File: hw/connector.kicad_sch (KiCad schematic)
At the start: 1 part, among them J1001 CONN_ECU_94

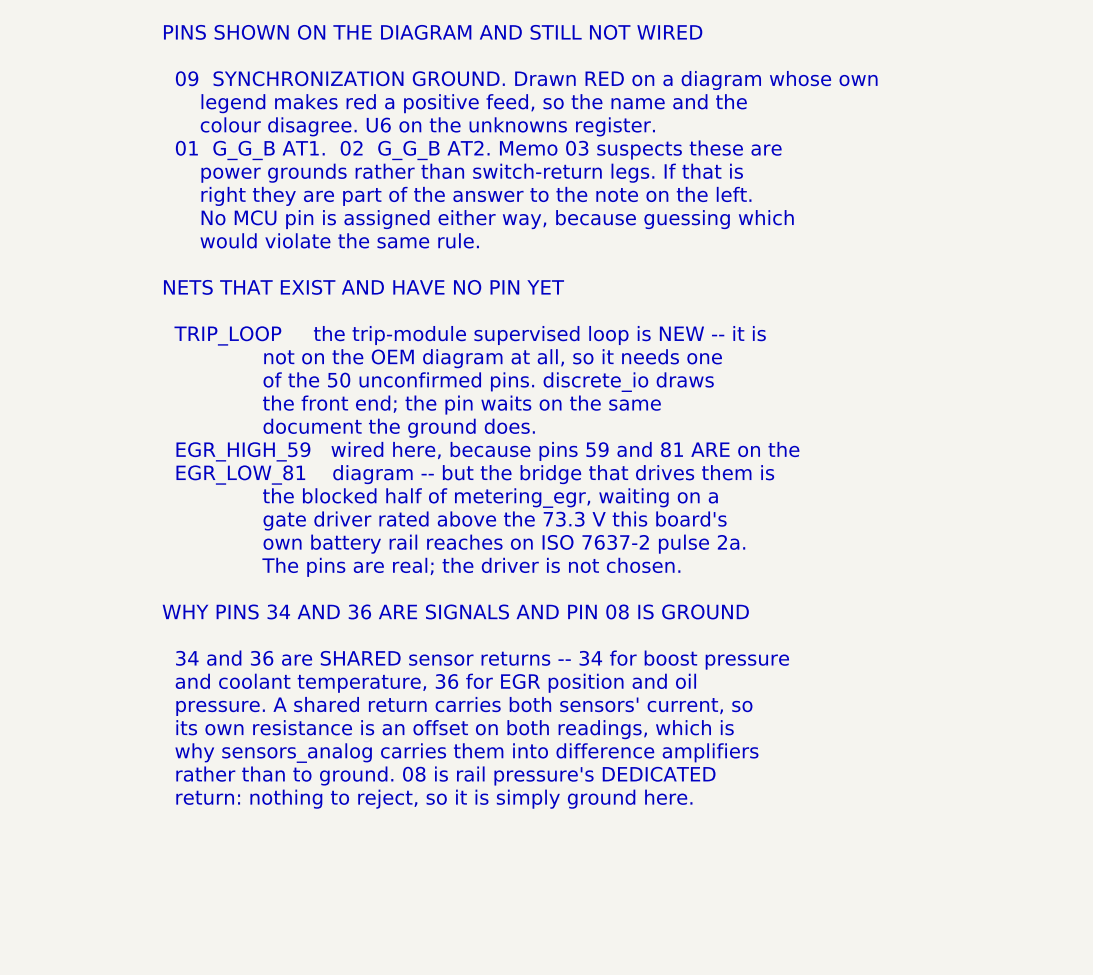
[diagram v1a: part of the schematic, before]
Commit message: Choose the buck inductor; record three design items the parts exposed
L201: Wurth 7447714330 (WE-PD 1050, 33 uH, Isat 2.9 A typ, AEC-Q200
Grade 1) -- 1.72x the 1.18 A worst peak after a -30% hot derate,
closing the Isat gap buck_preregulator.cir left open. Land pattern is
not in KiCad 7; phase 3.

Three items that are not part choices, each pinned as a check:
- POWER-PATH: injector and EGR current flows through pin 21, the EMI
  filter and a reverse FET sized for 5 A; pins 04/06 are 10 A battery
  feeds used only as senses. L101/L102/F101 wait on the decision.
- BOOST-SLOPE: by TI SLVS861F Eq. 9 the drawn 82 mOhm sense resistor
  exceeds the subharmonic ceiling at cranking (44.9 mOhm), and the
  330 uH it needs does not exist at a 2.2 A saturation rating.
- SENSOR-PTC: real PTCs are specified 0.40-5.00 ohm, not "3.0 ohm
  +/-30%", and Ihold halves at 85 C.

The netlist gate now counts the power ground as an open item: GND
reaches the connector only through sensor-ground pins. Removes a stale
EGR note from the connector sheet.

24/24 sim blocks, netlist gate passing with 2 named open items.
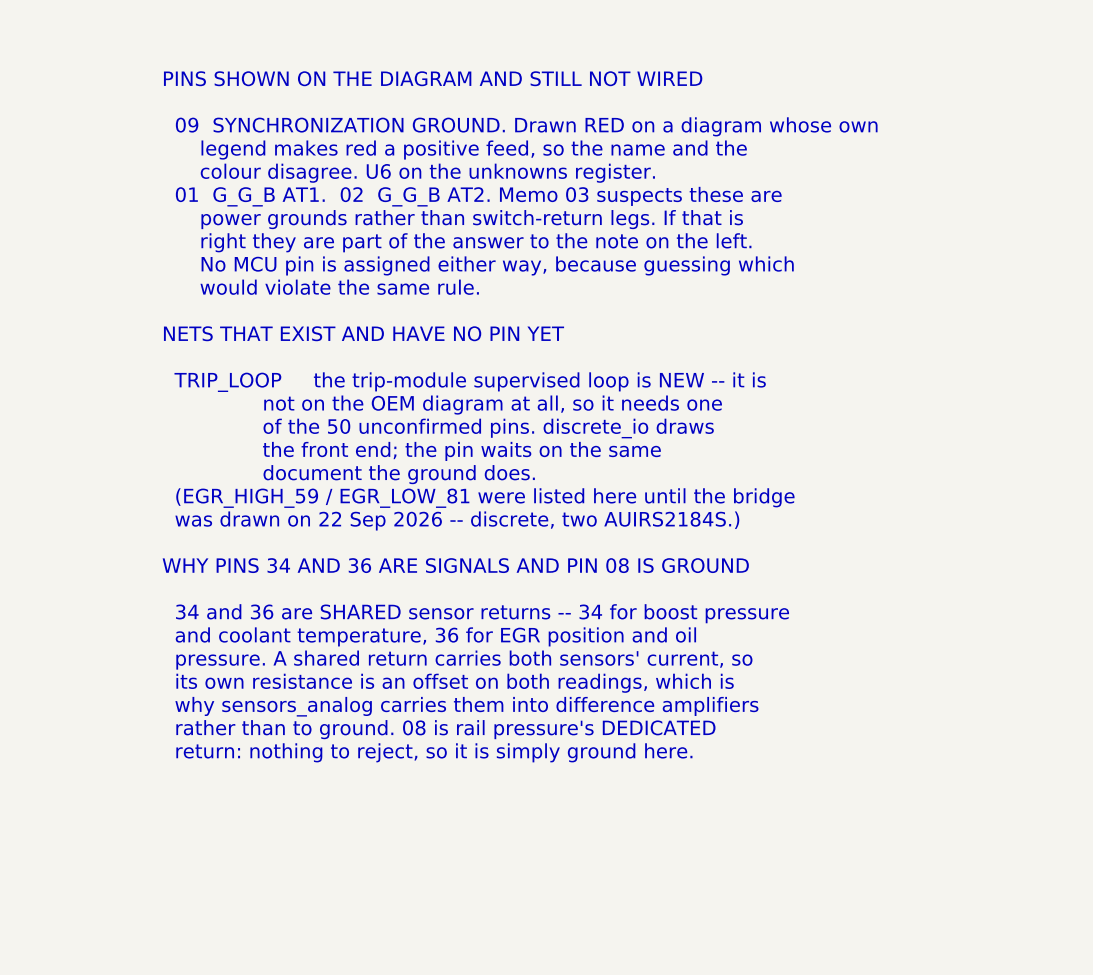
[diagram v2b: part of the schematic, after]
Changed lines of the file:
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@@
     (effects (font (size 1.6 1.6)) (justify left))
   )
-  (text "PINS SHOWN ON THE DIAGRAM AND STILL NOT WIRED\n\n  09  SYNCHRONIZATION GROUND. Drawn RED on a diagram whose own\n      legend makes red a positive feed, so the name and the\n      colour disagree. U6 on the unknowns register.\n  01  G_G_B AT1.  02  G_G_B AT2. Memo 03 suspects these are\n      power grounds rather than switch-return legs. If that is\n      right they are part of the answer to the note on the left.\n      No MCU pin is assigned either way, because guessing which\n      would violate the same rule.\n\nNETS THAT EXIST AND HAVE NO PIN YET\n\n  TRIP_LOOP     the trip-module supervised loop is NEW -- it is\n                not on the OEM diagram at all, so it needs one\n                of the 50 unconfirmed pins. discrete_io draws\n                the front end; the pin waits on the same\n                document the ground does.\n  EGR_HIGH_59   wired here, because pins 59 and 81 ARE on the\n  EGR_LOW_81    diagram -- but the bridge that drives them is\n                the blocked half of metering_egr, waiting on a\n                gate driver rated above the 73.3 V this board's\n                own battery rail reaches on ISO 7637-2 pulse 2a.\n                The pins are real; the driver is not chosen.\n\nWHY PINS 34 AND 36 ARE SIGNALS AND PIN 08 IS GROUND\n\n  34 and 36 are SHARED sensor returns -- 34 for boost pressure\n  and coolant temperature, 36 for EGR position and oil\n  pressure. A shared return carries both sensors' current, so\n  its own resistance is an offset on both readings, which is\n  why sensors_analog carries them into difference amplifiers\n  rather than to ground. 08 is rail pressure's DEDICATED\n  return: nothing to reject, so it is simply ground here." (at 400.0 130.0 0)
+  (text "PINS SHOWN ON THE DIAGRAM AND STILL NOT WIRED\n\n  09  SYNCHRONIZATION GROUND. Drawn RED on a diagram whose own\n      legend makes red a positive feed, so the name and the\n      colour disagree. U6 on the unknowns register.\n  01  G_G_B AT1.  02  G_G_B AT2. Memo 03 suspects these are\n      power grounds rather than switch-return legs. If that is\n      right they are part of the answer to the note on the left.\n      No MCU pin is assigned either way, because guessing which\n      would violate the same rule.\n\nNETS THAT EXIST AND HAVE NO PIN YET\n\n  TRIP_LOOP     the trip-module supervised loop is NEW -- it is\n                not on the OEM diagram at all, so it needs one\n                of the 50 unconfirmed pins. discrete_io draws\n                the front end; the pin waits on the same\n                document the ground does.\n  (EGR_HIGH_59 / EGR_LOW_81 were listed here until the bridge\n  was drawn on 22 Sep 2026 -- discrete, two AUIRS2184S.)\n\nWHY PINS 34 AND 36 ARE SIGNALS AND PIN 08 IS GROUND\n\n  34 and 36 are SHARED sensor returns -- 34 for boost pressure\n  and coolant temperature, 36 for EGR position and oil\n  pressure. A shared return carries both sensors' current, so\n  its own resistance is an offset on both readings, which is\n  why sensors_analog carries them into difference amplifiers\n  rather than to ground. 08 is rail pressure's DEDICATED\n  return: nothing to reject, so it is simply ground here." (at 400.0 130.0 0)
     (effects (font (size 1.6 1.6)) (justify left))
   )
